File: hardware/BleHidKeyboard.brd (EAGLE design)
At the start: 102 x 27.9 mm, 13 parts, among them IC1 MCP23018SSOP, IC2 MCP23018SSOP, J1 BATTERY, J4 KEYBOARD_2X13, U1 DYNASTREAM_N5150M5CD

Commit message: Switch to 1.2k LED current limiting resistors
This reduces current usage by half but still leaves them bright enough
to see.
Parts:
- R1, R2, R3: value 550 -> 1.2k
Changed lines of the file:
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@@
 <attribute name="NAME" x="97.8408" y="21.9202" size="0.508" layer="25" font="vector" rot="R180" align="center"/>
 </element>
-<element name="R1" library="rcl" package="R0805" value="550" x="61.214" y="26.289" smashed="yes">
+<element name="R1" library="rcl" package="R0805" value="1.2k" x="61.214" y="26.289" smashed="yes">
 <attribute name="NAME" x="63.9318" y="26.3144" size="0.508" layer="25" font="vector" align="center"/>
 </element>
-<element name="R2" library="rcl" package="R0805" value="550" x="79.375" y="26.289" smashed="yes">
+<element name="R2" library="rcl" package="R0805" value="1.2k" x="79.375" y="26.289" smashed="yes">
 <attribute name="NAME" x="76.6318" y="26.289" size="0.508" layer="25" font="vector" align="center"/>
 </element>
-<element name="R3" library="rcl" package="R0805" value="550" x="98.552" y="26.289" smashed="yes">
+<element name="R3" library="rcl" package="R0805" value="1.2k" x="98.552" y="26.289" smashed="yes">
 <attribute name="NAME" x="95.4786" y="26.3398" size="0.6096" layer="25" font="vector" align="center"/>
 </element>

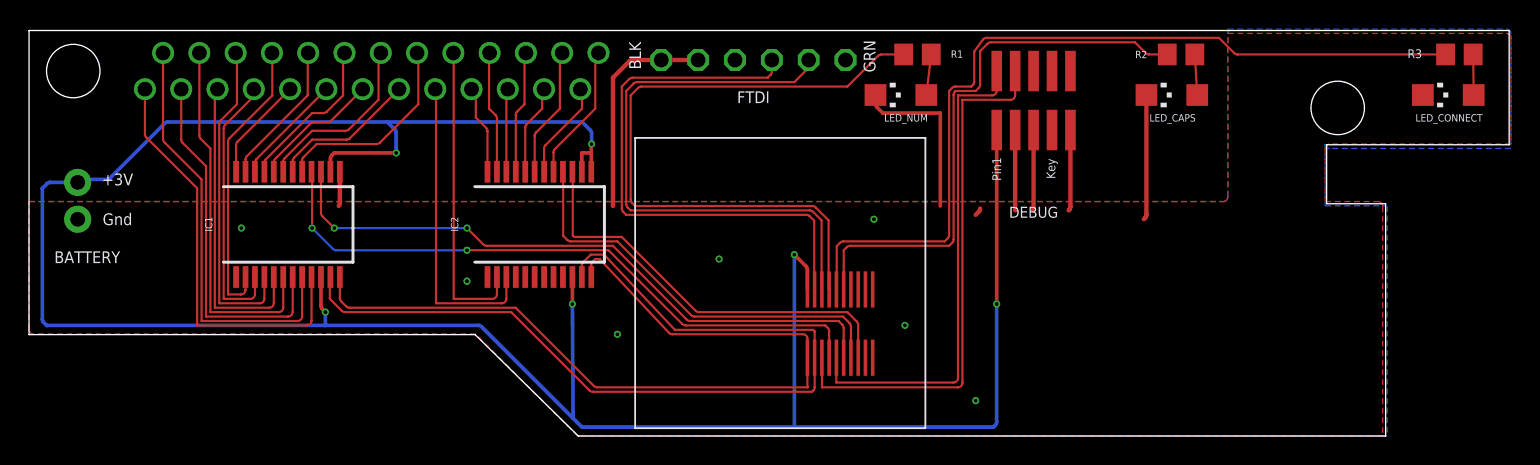
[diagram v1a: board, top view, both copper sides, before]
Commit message: Version 3 of the PCB design
This is the design being sent off to OSHPark on May 6th, 2018.

This version of the PCB no longer uses the 20-pin Molex connector on
the bottom of the Dynastream N5150M5CD module and instead uses the
pads around the perimeter of the N5150M4CD module (actually the same
module but without the Molex and SWD connectors) instead. The module
will now mount on the bottom of the PCB with the module can sticking up
through a hole in this new PCB. This will give us extra height
clearance and correct the problem that the current PCB doesn't fit in
the original keyboard case.

I updated the firmware to accomodate the change in pin mappings for
UART, I2C, LEDs, etc.
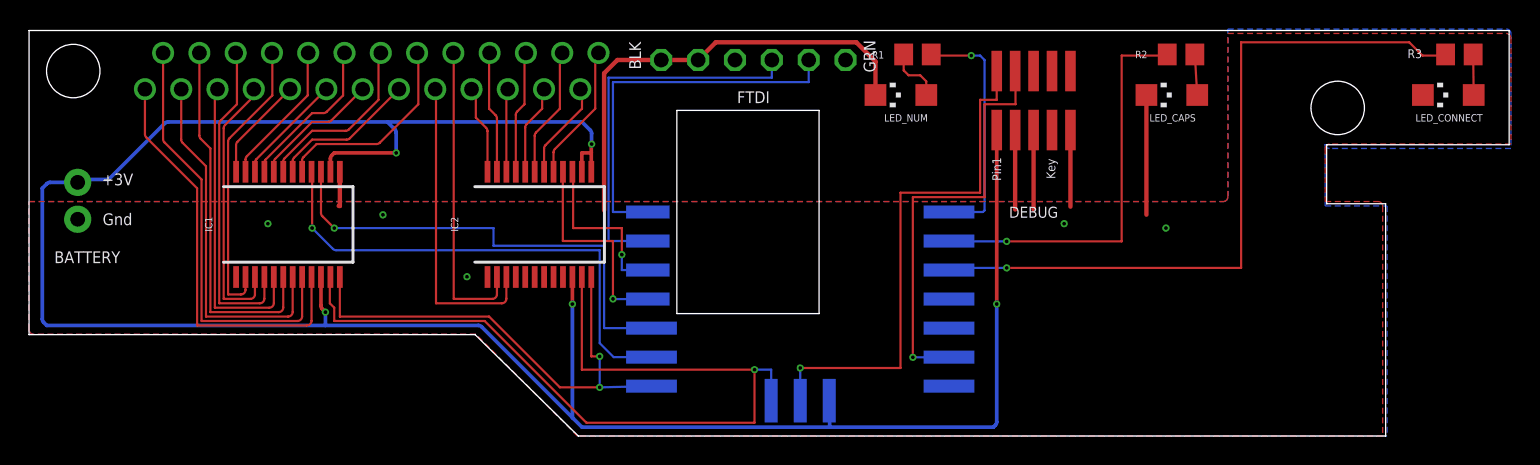
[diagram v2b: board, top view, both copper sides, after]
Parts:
- U1: value DYNASTREAM_N5150M5CD -> DYNASTREAM_N5150M4CD; device adam_custom:MOLEX_MINI_20POS -> adam_custom:N5150M4CD
- moved U1 5.43 mm to (53.1, 12.4)
- turned R1 to 180 degrees
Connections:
- net !RST/!SWDIO: now also U1.2; no longer U1.10
- net GND: now also U1.4; no longer U1.19
- net INTA-1: now also U1.16; no longer U1.8
- net INTB-1: now also U1.15; no longer U1.12
- net INTB-2: now also U1.13; no longer U1.16
- net LED_CAPS: now also U1.9; no longer U1.11
- net LED_CONNECT: now also U1.8; no longer U1.9
- net LED_NUM: now also U1.10; no longer U1.7
- net SCL: now also U1.1; no longer U1.4
- net SDA: now also U1.17; no longer U1.2
- net SWDCLK: now also U1.5; no longer U1.6
- net UART_RXD: now also U1.12; no longer U1.3
- net UART_TXD: now also U1.11; no longer U1.5
- net VCC: now also U1.3; no longer U1.1
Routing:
- net LED_NUM: track 46.2 -> 16.7 mm, vias 0 -> 1
- net SDA: track 57.9 -> 34.4 mm, vias 0 -> 2
- net INTB-2: track 28.9 -> 12.0 mm, vias 0 -> 1
- net INTA-2: track 29.0 -> 14.7 mm, vias 0 -> 1
- net UART_TXD: track 40.3 -> 26.4 mm
- net VCC: track 178.7 -> 165.8 mm, vias 6 -> 5
- net UART_RXD: track 38.4 -> 26.4 mm
- net INTB-1: track 44.2 -> 33.0 mm, vias 2 -> 1
- net LED_CAPS: track 38.6 -> 27.9 mm, vias 0 -> 1
- net INTA-1: track 44.3 -> 34.7 mm, vias 2 -> 1
- net LED_CONNECT: track 58.5 -> 50.3 mm, vias 0 -> 1
- net SWDCLK: track 36.8 -> 29.3 mm, vias 0 -> 1
- net GND: track 55.2 -> 58.8 mm, vias 7 -> 5
- net !RST/!SWDIO: track 33.9 -> 36.2 mm, vias 0 -> 1
- net N$1: track 2.81 -> 3.91 mm
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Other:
- board text added: "Version 3"
- board text removed: "Version 1"
